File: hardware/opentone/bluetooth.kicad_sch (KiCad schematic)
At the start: 1 part

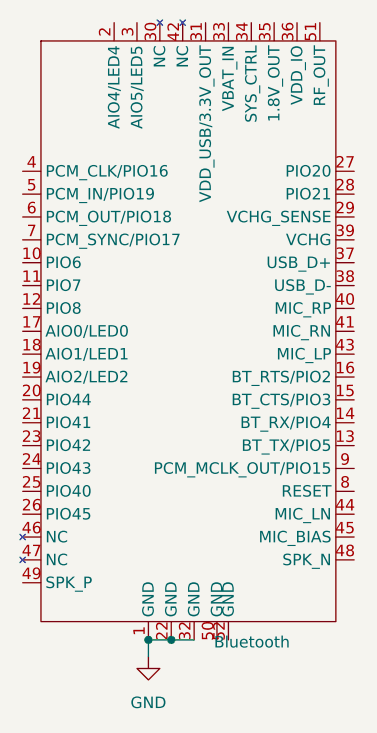
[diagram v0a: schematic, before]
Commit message: Rename (#3)
* added dot when on a page with blank characters

* rename

* actions only on new version tag on master
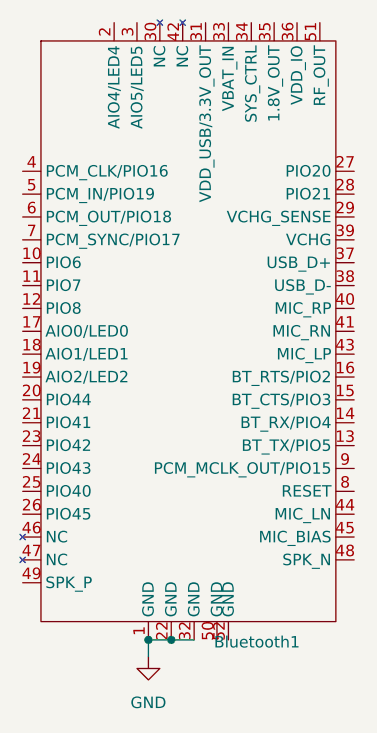
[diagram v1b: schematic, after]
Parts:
- Bluetooth1: renamed from Bluetooth; footprint openpod:fsc-bt1035 -> opentone:fsc-bt1035; symbol openpod:FSC-BT1035 -> opentone:FSC-BT1035
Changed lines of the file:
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@@
 		)
 		(instances
-			(project "openpod"
+			(project "opentone"
 				(path "/0122bb8c-dbef-4db1-a6c6-9be780a38d9f/cd416ea8-5a7a-445f-9d82-6d6499825b26"
 					(reference "#PWR025")
@@
 	)
 	(symbol
-		(lib_id "openpod:FSC-BT1035")
+		(lib_id "opentone:FSC-BT1035")
 		(at 182.245 73.66 0)
 		(unit 1)
@@
 		(dnp no)
 		(fields_autoplaced yes)
-		(property "Reference" "Bluetooth"
+		(property "Reference" "Bluetooth1"
 			(at 185.7091 127.254 0)
 			(effects
@@
 			)
 		)
-		(property "Footprint" "openpod:fsc-bt1035"
+		(property "Footprint" "opentone:fsc-bt1035"
 			(at 200.025 69.85 0)
 			(effects
@@
 		)
 		(instances
-			(project "openpod"
+			(project "opentone"
 				(path "/0122bb8c-dbef-4db1-a6c6-9be780a38d9f/cd416ea8-5a7a-445f-9d82-6d6499825b26"
-					(reference "Bluetooth")
+					(reference "Bluetooth1")
 					(unit 1)
 				)
